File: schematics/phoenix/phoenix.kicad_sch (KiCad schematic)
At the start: 3 parts, among them U1 MAX31856

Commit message: schematic updates
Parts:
- removed DS1: HY1602E, Display:HY1602E, symbol Display_Character:HY1602E
- added U2: NHD-C0220BIZ, Package_DIP:DIP-20_W7.62mm_Socket, symbol Display_Character:NHD-C0220BIZ
- added U3: HHG1D-1, Relay_THT:Relay_NCR_HHG1D-1, symbol Relay_SolidState:HHG1D-1
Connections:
- net at U1.1 (AGND): now also A1.29 (GND), U1.14 (DGND), U2.4 (VSS)
- net SCK: now reaches U1.10 (SCK)
- net SCK: now also A1.28 (D13)
- net MISO: now reaches U1.11 (SDO)
- net MISO: now also A1.27 (D12)
- net MOSI: now reaches U1.12 (SDI)
- net MOSI: now also A1.26 (D11)
- net at U1.5 (AVDD): now also A1.5 (+5V), U1.8 (DVDD), U2.5 (VDD)
- net ~{DRDY}: now reaches U1.7 (~{DRDY})
- net ~{DRDY}: now also A1.20 (D5)
- net ~{CS}: now reaches U1.9 (~{CS})
- net ~{CS}: now also A1.25 (D10)
- net at A1.13 (SDA/A4): now also U2.3 (SDA)
- net at A1.14 (SCL/A5): now also U2.2 (SCL)
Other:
- moved on the sheet: A1, U1

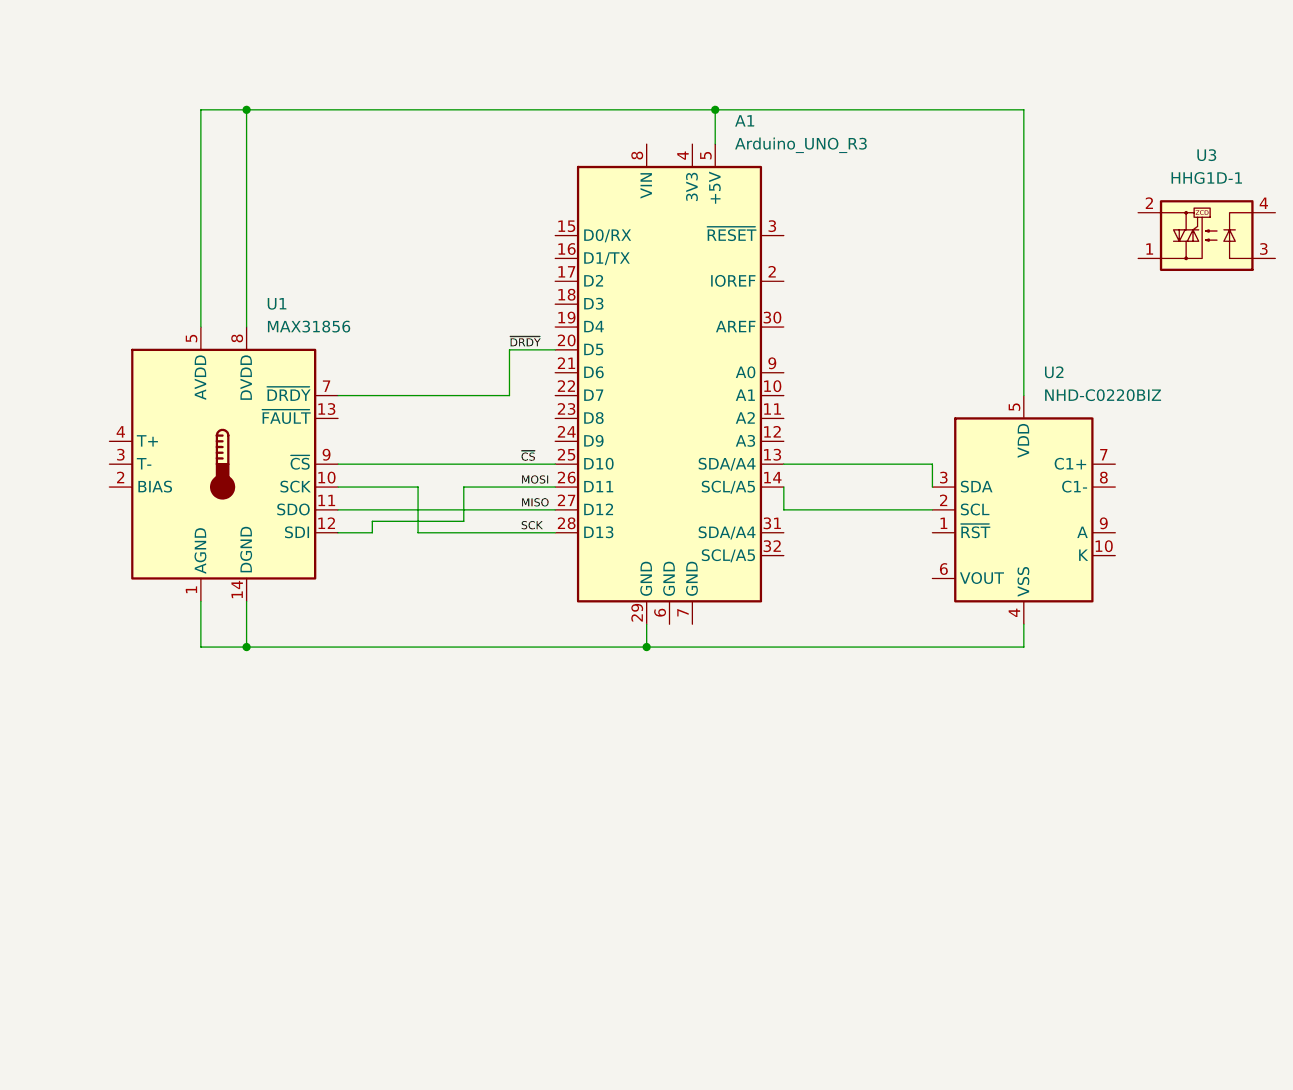
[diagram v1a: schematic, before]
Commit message: added ssr connection to schematic
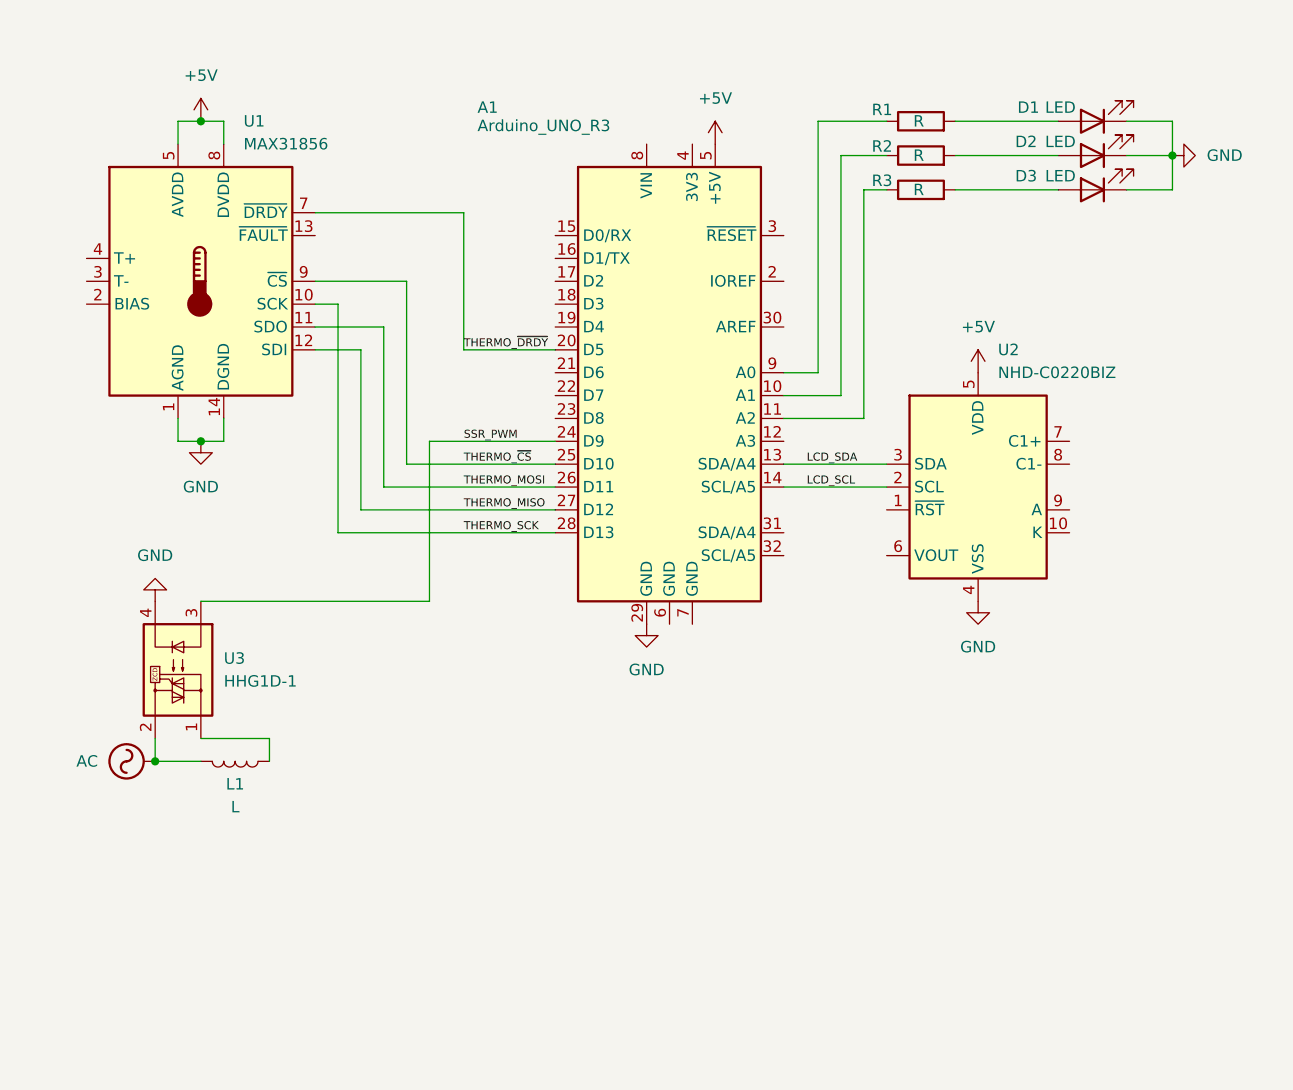
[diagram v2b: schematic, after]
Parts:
- added D1, D2, D3: LED, symbol Device:LED
- added L1: L, symbol Device:L
- added R1, R2, R3: R, symbol Device:R
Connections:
- net GND: now reaches A1.29 (GND), U1.1 (AGND), U1.14 (DGND), U2.4 (VSS)
- net GND: now also U3.4, D1.1 (K), D2.1 (K), D3.1 (K)
- net +5V: now reaches A1.5 (+5V), U1.5 (AVDD), U1.8 (DVDD), U2.5 (VDD)
- net LCD_SCL: now reaches A1.14 (SCL/A5), U2.2 (SCL)
- net LCD_SDA: now reaches A1.13 (SDA/A4), U2.3 (SDA)
- net at A1.10 (A1): now also R2.1
- net at A1.11 (A2): now also R3.1
- net SSR_PWM: now reaches A1.24 (D9)
- net SSR_PWM: now also U3.3
- net at A1.9 (A0): now also R1.1
- net at U3.1: now also L1.1
- net AC: now reaches U3.2
- net AC: now also L1.2
- net MISO renamed THERMO_MISO
- net THERMO_MISO: now also U1.12 (SDI); no longer U1.11 (SDO)
- net MOSI renamed THERMO_MOSI
- net THERMO_MOSI: now also U1.11 (SDO); no longer U1.12 (SDI)
- net SCK renamed THERMO_SCK
- net ~{CS} renamed THERMO_~{CS}
- net ~{DRDY} renamed THERMO_~{DRDY}
- new net: D1.2 (A), R1.2
- new net: D3.2 (A), R3.2
- new net: D2.2 (A), R2.2
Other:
- moved on the sheet: U1, U2, U3

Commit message: schematic done probably
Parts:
- added SW1: RotaryEncoder, symbol Device:RotaryEncoder
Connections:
- net GND: now also SW1.C
- net THERMO_MISO: now also U1.11 (SDO); no longer U1.12 (SDI)
- net THERMO_MOSI: now also U1.12 (SDI); no longer U1.11 (SDO)
- net at A1.17 (D2): now also SW1.A
- net at A1.18 (D3): now also SW1.B
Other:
- title: (none) -> Phoenix - Tube Furnace
- moved on the sheet: L1, U1, U3
